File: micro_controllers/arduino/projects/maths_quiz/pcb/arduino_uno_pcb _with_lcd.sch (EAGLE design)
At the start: 13 parts, among them IC1 ATMEGA328, Q1 16MHZ

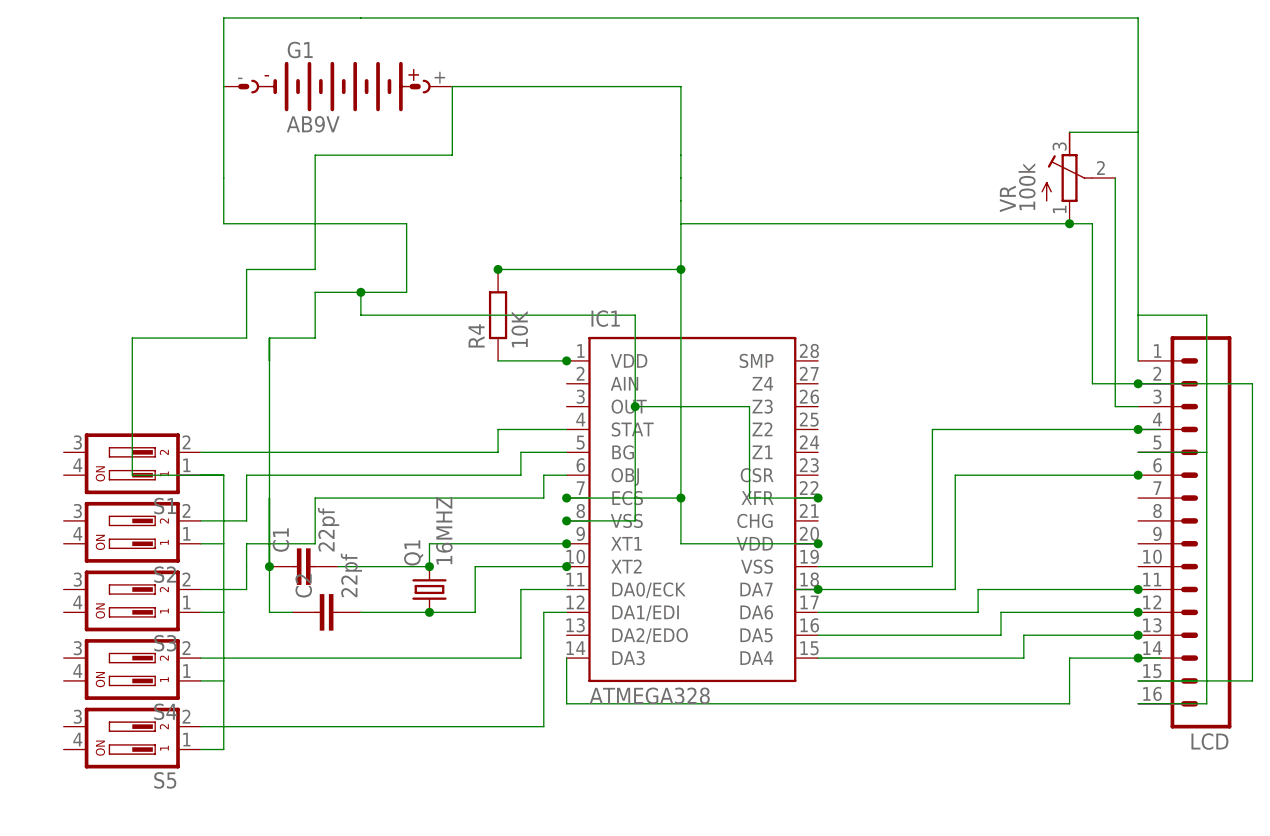
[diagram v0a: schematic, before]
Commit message: 
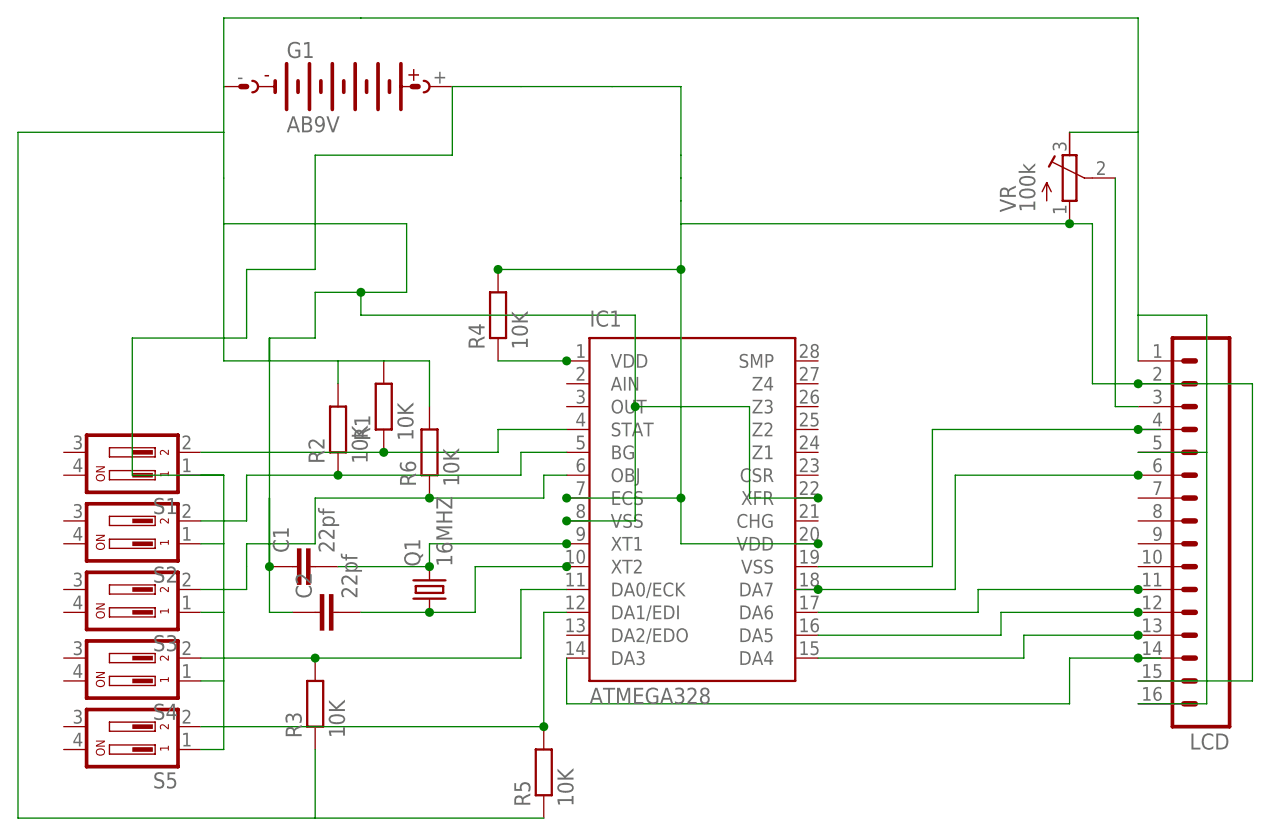
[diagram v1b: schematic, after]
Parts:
- added R1, R2, R3, R5, R6: 10K, rcl:R-EU_0207/10
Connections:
- removed net N$28: C1.1, C2.1, G1.-, IC1.VSS, IC1.XFR, LCD.1, LCD.16, LCD.5, VR.A
- new net N$6: C1.1, C2.1, G1.-, IC1.VSS, IC1.XFR, LCD.1, LCD.16, LCD.5, R1.2, R2.2, R3.1, R5.1, R6.2, VR.A
- net N$4: now also R3.2
- net N$5: now also R1.1
- net N$7: now also R2.1
- net N$8: now also R6.1
- net N$9: now also R5.2
